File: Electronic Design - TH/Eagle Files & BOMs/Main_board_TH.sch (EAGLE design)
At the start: 46 parts, among them IC2 ATMEGA328-PU, X1 16MHz

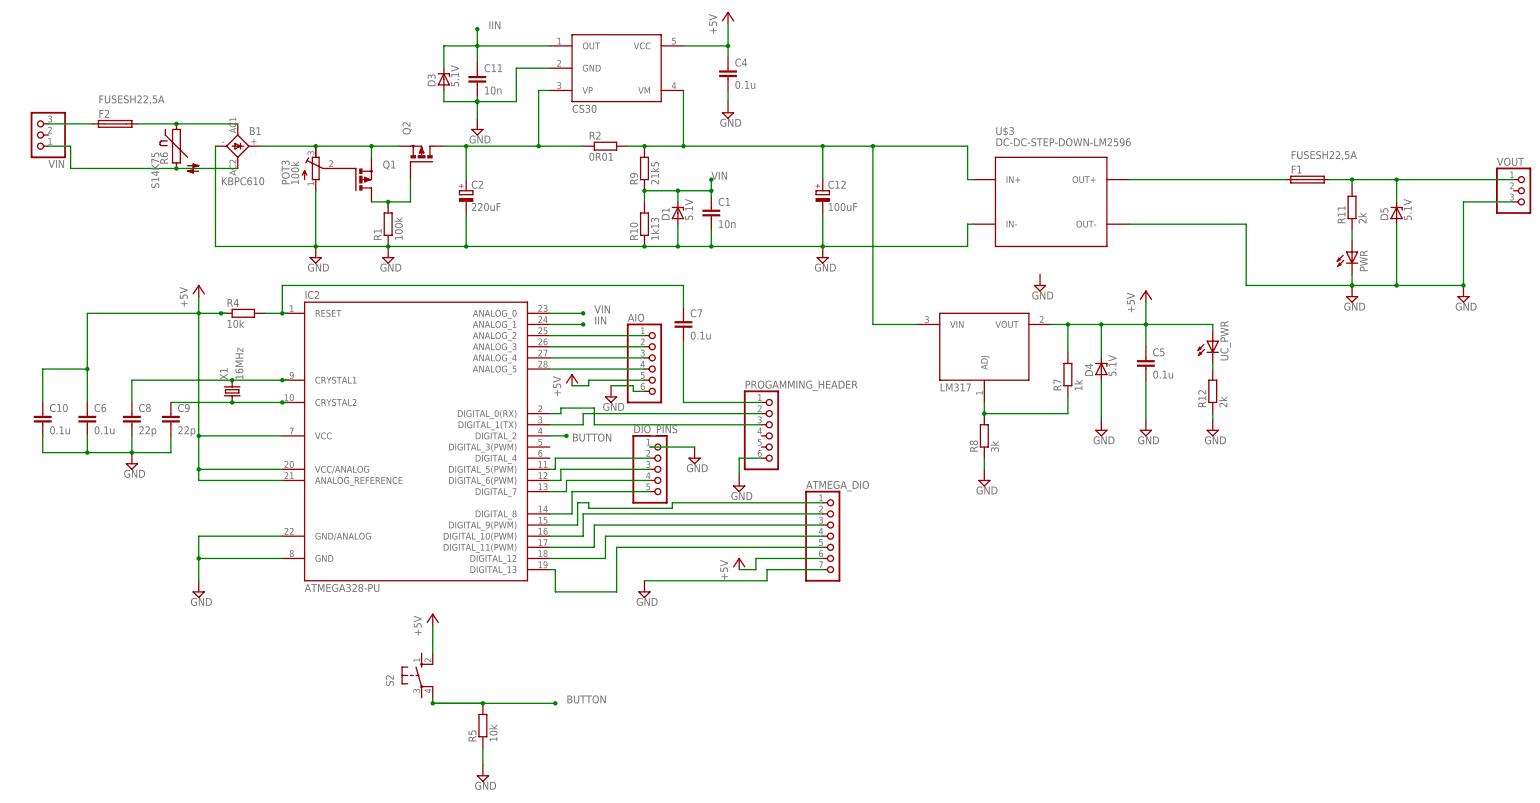
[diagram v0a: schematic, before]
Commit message: renamed files to reflect two versions of L.E.One and replacing ATmega 328 with arduino nano
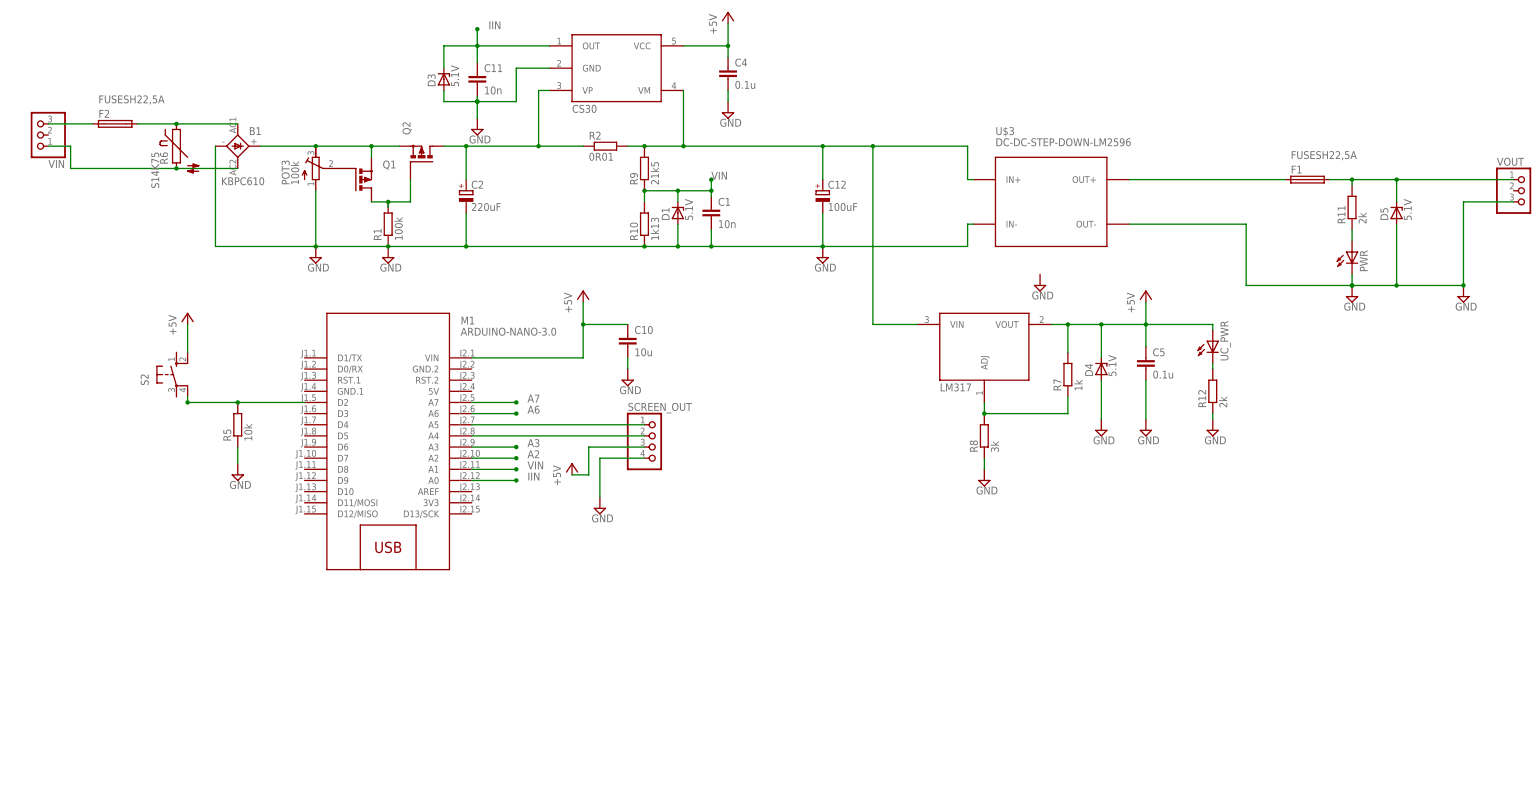
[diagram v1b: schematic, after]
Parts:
- removed AIO, PROGAMMING_HEADER: (no value), pinhead:PINHD-1X6
- removed ATMEGA_DIO: (no value), pinhead:PINHD-1X7
- removed C6, C7: 0.1u, resistor:C-EU050-024X044
- removed C8, C9: 22p, resistor:C-EU050-024X044
- removed DIO_PINS: (no value), pinhead:PINHD-1X5
- removed IC2: ATMEGA328-PU, Arduino-AVR:ATMEGA168-PU
- removed R4: 10k, resistor:R-EU_0207/10
- removed X1: 16MHz, crystal:CRYSTALHC49S
- added M1: ARDUINO-NANO-3.0, diy-modules:ARDUINO-NANO-3.0
- added SCREEN_OUT: (no value), pinhead:PINHD-1X4
- C10: value 0.1u -> 10u
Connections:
- removed net ANALOG_2: AIO.1, IC2.ANALOG_2
- removed net ANALOG_3: AIO.2, IC2.ANALOG_3
- removed net ANALOG_4: AIO.3, IC2.ANALOG_4
- removed net ANALOG_5: AIO.4, IC2.ANALOG_5
- removed net CRYSTAL1: C8.1, IC2.CRYSTAL1, X1.2
- removed net CRYSTAL2: C9.1, IC2.CRYSTAL2, X1.1
- removed net D10: ATMEGA_DIO.2, IC2.DIGITAL_10(PWM)
- removed net D11: ATMEGA_DIO.3, IC2.DIGITAL_11(PWM)
- removed net D12: ATMEGA_DIO.4, IC2.DIGITAL_12
- removed net D13: ATMEGA_DIO.5, IC2.DIGITAL_13
- removed net D5: DIO_PINS.2, IC2.DIGITAL_5(PWM)
- removed net D6: DIO_PINS.3, IC2.DIGITAL_6(PWM)
- removed net D7: DIO_PINS.4, IC2.DIGITAL_7
- removed net D8: DIO_PINS.5, IC2.DIGITAL_8
- removed net D9: ATMEGA_DIO.1, IC2.DIGITAL_9(PWM)
- removed net N$14: C7.2, PROGAMMING_HEADER.1
- removed net N$4: IC2.DIGITAL_1(TX), PROGAMMING_HEADER.2
- removed net N$5: IC2.DIGITAL_0(RX), PROGAMMING_HEADER.3
- removed net RESET: C7.1, IC2.RESET, R4.2
- new net A2: M1.A2
- new net A3: M1.A3
- new net A6: M1.A6
- new net A7: M1.A7
- new net N$2: M1.A4, SCREEN_OUT.2
- new net N$3: M1.A5, SCREEN_OUT.1
- net +5V: now also M1.VIN, SCREEN_OUT.3; no longer AIO.5, ATMEGA_DIO.6, C6.1, IC2.ANALOG_REFERENCE, IC2.VCC, IC2.VCC/ANALOG, R4.1
- net BUTTON: now also M1.D2; no longer IC2.DIGITAL_2
- net GND: now also SCREEN_OUT.4; no longer AIO.6, ATMEGA_DIO.7, C6.2, C8.2, C9.2, DIO_PINS.1, IC2.GND, IC2.GND/ANALOG, PROGAMMING_HEADER.6
- net IIN: no longer IC2.ANALOG_1
- net VIN: no longer IC2.ANALOG_0
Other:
- moved on the sheet: C10, R5, S2

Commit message: replacing CS30 with LM358
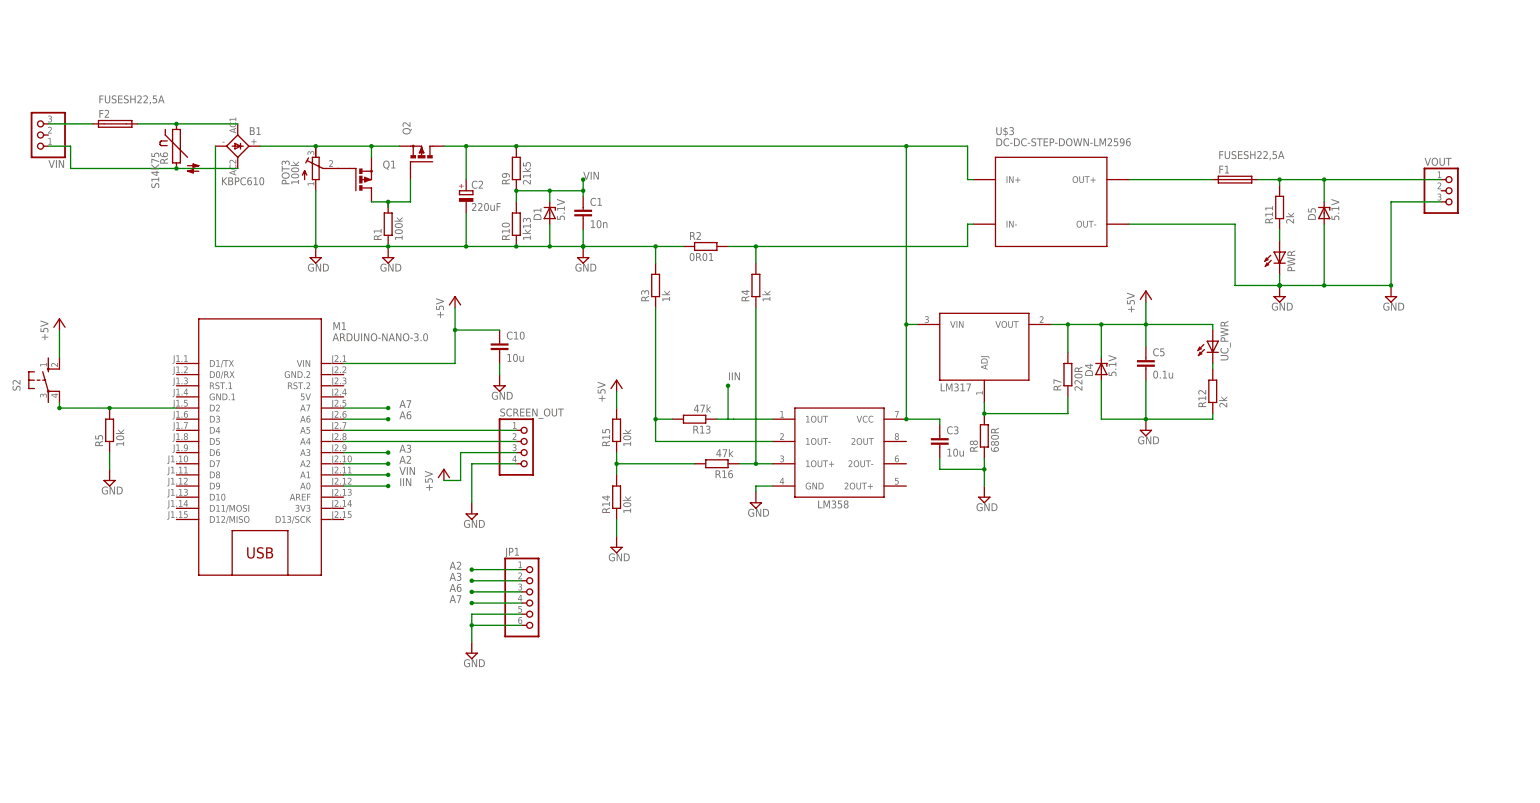
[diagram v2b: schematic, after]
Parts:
- removed C11: 10n, resistor:C-EU050-024X044
- removed C12: 100uF, resistor:CPOL-EUE3.5-8
- removed C4: 0.1u, resistor:C-EU050-024X044
- removed D3: 5.1V, diode:ZPD
- added C3: 10u, resistor:C-EU050-024X044
- added JP1: (no value), pinhead:PINHD-1X6
- added R13, R16: 47k, resistor:R-EU_0207/10
- added R14, R15: 10k, resistor:R-EU_0207/10
- added R3, R4: 1k, resistor:R-EU_0207/10
- R7: value 1k -> 220R
- R8: value 3k -> 680R
- U$2: value CS30 -> LM358; device Samson:CS30 -> Samson:LM358
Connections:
- removed net VIN_CURRENT_MEASURED: C12.+, R2.2, R9.2, U$1.VIN, U$2.VM, U$3.IN+
- new net N$4: R2.2, R4.2, U$3.IN-
- new net N$5: R16.1, R4.1, U$2.1OUT+
- new net N$6: R13.2, R3.1, U$2.1OUT-
- new net N$8: R14.2, R15.1, R16.2
- net +5V: now also R15.2; no longer C4.1, U$2.VCC
- net A2: now also JP1.1
- net A3: now also JP1.2
- net A6: now also JP1.3
- net A7: now also JP1.4
- net GND: now also C3.2, JP1.5, JP1.6, R14.1, R2.1, R3.2; no longer C11.2, C12.-, C4.2, D3.A, U$3.IN-
- net IIN: now also M1.A0, R13.1, U$2.1OUT; no longer C11.1, D3.C, U$2.OUT
- net VIN: now also M1.A1
- net VIN_PROTECTED: now also C3.1, R9.2, U$1.VIN, U$2.VCC, U$3.IN+; no longer R2.1, U$2.VP
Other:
- moved on the sheet: C1, C10, D1, D5, F1, M1, PWR, R10, R11, R2, R5, R9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

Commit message: replacing divider resistors for voltage measurement
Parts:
- R10: value 1k13 -> 1k
- R9: value 21k5 -> 10k
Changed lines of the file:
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@@
 <part name="C5" library="resistor" deviceset="C-EU" device="050-024X044" value="0.1u"/>
 <part name="SUPPLY11" library="supply2" deviceset="GND" device=""/>
-<part name="R9" library="resistor" deviceset="R-EU_" device="0207/10" value="21k5"/>
-<part name="R10" library="resistor" deviceset="R-EU_" device="0207/10" value="1k13"/>
+<part name="R9" library="resistor" deviceset="R-EU_" device="0207/10" value="10k"/>
+<part name="R10" library="resistor" deviceset="R-EU_" device="0207/10" value="1k"/>
 <part name="SUPPLY12" library="supply2" deviceset="GND" device=""/>
 <part name="D4" library="diode" deviceset="ZPD" device="" value="5.1V"/>

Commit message: Adding names of Q1 and Q2
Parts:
- Q1, Q2: value (none) -> IRF9520
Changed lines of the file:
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@@
 <setting verticaltext="up"/>
 </settings>
-<grid distance="0.05" unitdist="inch" unit="inch" style="lines" multiple="1" display="no" altdistance="0.01" altunitdist="inch" altunit="inch"/>
+<grid distance="0.1" unitdist="inch" unit="inch" style="lines" multiple="1" display="no" altdistance="0.01" altunitdist="inch" altunit="inch"/>
 <layers>
 <layer number="1" name="Top" color="4" fill="1" visible="no" active="no"/>
@@
 <part name="R11" library="resistor" deviceset="R-EU_" device="0207/10" value="2k"/>
 <part name="R12" library="resistor" deviceset="R-EU_" device="0207/10" value="2k"/>
-<part name="Q1" library="Samson" deviceset="PMOSFET_P" device="TO220BH"/>
-<part name="Q2" library="Samson" deviceset="PMOSFET_P" device="TO220BH"/>
+<part name="Q1" library="Samson" deviceset="PMOSFET_P" device="TO220BH" value="IRF9520"/>
+<part name="Q2" library="Samson" deviceset="PMOSFET_P" device="TO220BH" value="IRF9520"/>
 <part name="F2" library="fuse" deviceset="FUSE" device="SH22,5A" value="FUSESH22,5A"/>
 <part name="U$3" library="diy-modules" deviceset="DC-DC-STEP-DOWN-LM2596" device=""/>

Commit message: adding ground to arduino
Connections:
- net GND: now also M1.GND.2
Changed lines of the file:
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@@
 <setting verticaltext="up"/>
 </settings>
-<grid distance="0.1" unitdist="inch" unit="inch" style="lines" multiple="1" display="no" altdistance="0.01" altunitdist="inch" altunit="inch"/>
+<grid distance="0.05" unitdist="inch" unit="inch" style="lines" multiple="1" display="no" altdistance="0.01" altunitdist="inch" altunit="inch"/>
 <layers>
 <layer number="1" name="Top" color="4" fill="1" visible="no" active="no"/>
@@
 <part name="SUPPLY5" library="supply2" deviceset="GND" device=""/>
 <part name="C3" library="resistor" deviceset="C-EU" device="050-024X044" value="10u"/>
+<part name="SUPPLY6" library="supply2" deviceset="GND" device=""/>
 </parts>
 <sheets>
@@
 <instance part="SUPPLY5" gate="GND" x="-30.48" y="-26.67"/>
 <instance part="C3" gate="G$1" x="76.2" y="22.86"/>
+<instance part="SUPPLY6" gate="GND" x="-34.29" y="33.02"/>
 </instances>
 <busses>
@@
 <junction x="27.94" y="34.29"/>
 <label x="27.94" y="35.56" size="1.778" layer="95"/>
+<junction x="27.94" y="26.67"/>
 </segment>
 </net>
@@
 <junction x="-30.48" y="-20.32"/>
 </segment>
+<segment>
+<pinref part="M1" gate="G$1" pin="GND.2"/>
+<pinref part="SUPPLY6" gate="GND" pin="GND"/>
+<wire x1="-59.69" y1="36.83" x2="-34.29" y2="36.83" width="0.1524" layer="91"/>
+<wire x1="-34.29" y1="36.83" x2="-34.29" y2="35.56" width="0.1524" layer="91"/>
+</segment>
 </net>

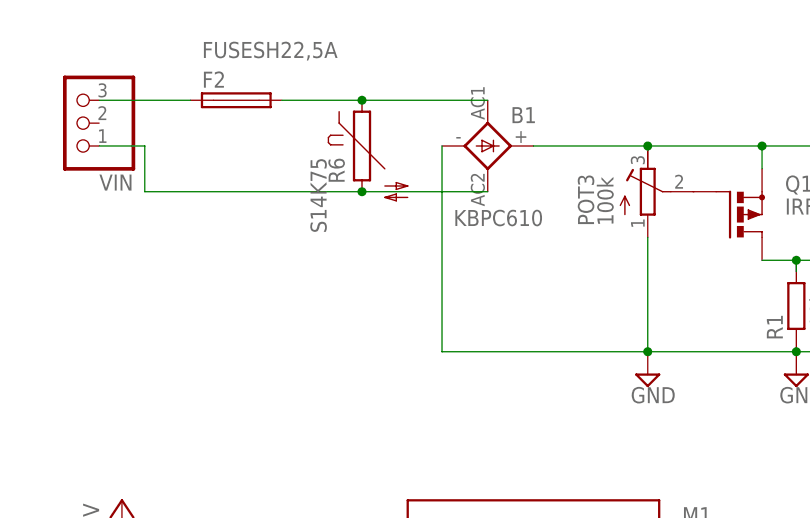
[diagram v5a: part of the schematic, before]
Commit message: Moving varistor to after rectification stage
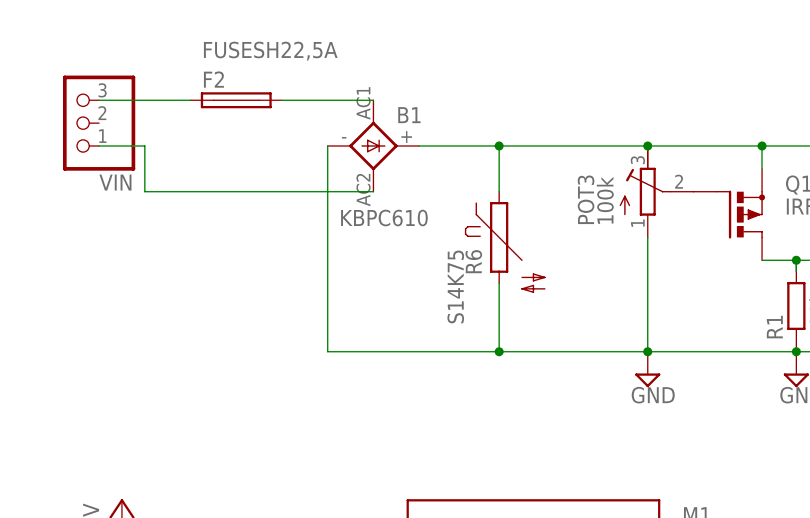
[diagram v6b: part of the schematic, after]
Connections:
- removed net VIN_AC1: B1.AC1, F2.2, R6.1
- removed net VIN_AC2: B1.AC2, R6.2, VIN.1
- new net N$7: B1.AC2, VIN.1
- new net N$9: B1.AC1, F2.2
- net GND: now also R6.2
- net VIN_UNPROTECTED: now also R6.1
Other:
- moved on the sheet: B1, R6
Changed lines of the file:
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@@
 </plain>
 <instances>
-<instance part="B1" gate="1" x="-83.82" y="88.9" smashed="yes">
-<attribute name="NAME" x="-81.28" y="91.44" size="1.778" layer="95"/>
-<attribute name="VALUE" x="-87.63" y="80.01" size="1.778" layer="96"/>
+<instance part="B1" gate="1" x="-96.52" y="88.9" smashed="yes">
+<attribute name="NAME" x="-93.98" y="91.44" size="1.778" layer="95"/>
+<attribute name="VALUE" x="-100.33" y="80.01" size="1.778" layer="96"/>
 </instance>
 <instance part="C1" gate="G$1" x="-5.08" y="74.93"/>
@@
 <instance part="SUPPLY3" gate="GND" x="-113.03" y="12.7"/>
 <instance part="D1" gate="G$1" x="-12.7" y="73.66" rot="R90"/>
-<instance part="R6" gate="G$1" x="-97.79" y="88.9" rot="R270"/>
+<instance part="R6" gate="G$1" x="-82.55" y="78.74" rot="R270"/>
 <instance part="SUPPLY2" gate="GND" x="179.07" y="54.61"/>
 <instance part="SUPPLY4" gate="GND" x="86.36" y="8.89"/>
@@
 <junction x="-66.04" y="66.04"/>
 <pinref part="B1" gate="1" pin="-"/>
-<wire x1="-88.9" y1="88.9" x2="-88.9" y2="66.04" width="0.1524" layer="91"/>
-<wire x1="-66.04" y1="66.04" x2="-88.9" y2="66.04" width="0.1524" layer="91"/>
+<wire x1="-101.6" y1="88.9" x2="-101.6" y2="66.04" width="0.1524" layer="91"/>
+<wire x1="-66.04" y1="66.04" x2="-82.55" y2="66.04" width="0.1524" layer="91"/>
+<wire x1="-82.55" y1="66.04" x2="-101.6" y2="66.04" width="0.1524" layer="91"/>
 <wire x1="-12.7" y1="66.04" x2="-5.08" y2="66.04" width="0.1524" layer="91"/>
 <wire x1="-12.7" y1="71.12" x2="-12.7" y2="66.04" width="0.1524" layer="91"/>
@@
 <wire x1="11.43" y1="62.23" x2="11.43" y2="66.04" width="0.1524" layer="91"/>
 <junction x="11.43" y="66.04"/>
+<pinref part="R6" gate="G$1" pin="2"/>
+<wire x1="-82.55" y1="73.66" x2="-82.55" y2="66.04" width="0.1524" layer="91"/>
+<junction x="-82.55" y="66.04"/>
 </segment>
 <segment>
@@
 <pinref part="B1" gate="1" pin="+"/>
 <wire x1="-53.34" y1="88.9" x2="-46.99" y2="88.9" width="0.1524" layer="91"/>
-<wire x1="-78.74" y1="88.9" x2="-66.04" y2="88.9" width="0.1524" layer="91"/>
+<wire x1="-91.44" y1="88.9" x2="-82.55" y2="88.9" width="0.1524" layer="91"/>
 <junction x="-66.04" y="88.9"/>
 <pinref part="Q2" gate="G$1" pin="S"/>
 <pinref part="Q1" gate="G$1" pin="S"/>
+<wire x1="-82.55" y1="88.9" x2="-66.04" y2="88.9" width="0.1524" layer="91"/>
 <wire x1="-53.34" y1="86.36" x2="-53.34" y2="88.9" width="0.1524" layer="91"/>
 <junction x="-53.34" y="88.9"/>
+<pinref part="R6" gate="G$1" pin="1"/>
+<wire x1="-82.55" y1="88.9" x2="-82.55" y2="83.82" width="0.1524" layer="91"/>
+<junction x="-82.55" y="88.9"/>
 </segment>
 </net>
@@
 </segment>
 </net>
-<net name="VIN_AC2" class="0">
-<segment>
-<pinref part="VIN" gate="A" pin="1"/>
-<wire x1="-127" y1="88.9" x2="-121.92" y2="88.9" width="0.1524" layer="91"/>
-<wire x1="-121.92" y1="88.9" x2="-121.92" y2="83.82" width="0.1524" layer="91"/>
-<pinref part="R6" gate="G$1" pin="2"/>
-<wire x1="-121.92" y1="83.82" x2="-97.79" y2="83.82" width="0.1524" layer="91"/>
-<pinref part="B1" gate="1" pin="AC2"/>
-<wire x1="-97.79" y1="83.82" x2="-83.82" y2="83.82" width="0.1524" layer="91"/>
-<junction x="-97.79" y="83.82"/>
-</segment>
-</net>
 <net name="N$23" class="0">
 <segment>
@@
 </segment>
 </net>
-<net name="VIN_AC1" class="0">
-<segment>
-<pinref part="R6" gate="G$1" pin="1"/>
-<pinref part="B1" gate="1" pin="AC1"/>
-<wire x1="-83.82" y1="93.98" x2="-97.79" y2="93.98" width="0.1524" layer="91"/>
-<pinref part="F2" gate="G$1" pin="2"/>
-<wire x1="-106.68" y1="93.98" x2="-97.79" y2="93.98" width="0.1524" layer="91"/>
-<junction x="-97.79" y="93.98"/>
-</segment>
-</net>
 <net name="VOUT_PREFUSE" class="0">
 <segment>
@@
 </segment>
 </net>
+<net name="N$7" class="0">
+<segment>
+<pinref part="VIN" gate="A" pin="1"/>
+<wire x1="-127" y1="88.9" x2="-121.92" y2="88.9" width="0.1524" layer="91"/>
+<wire x1="-121.92" y1="88.9" x2="-121.92" y2="83.82" width="0.1524" layer="91"/>
+<pinref part="B1" gate="1" pin="AC2"/>
+<wire x1="-121.92" y1="83.82" x2="-96.52" y2="83.82" width="0.1524" layer="91"/>
+</segment>
+</net>
+<net name="N$9" class="0">
+<segment>
+<pinref part="B1" gate="1" pin="AC1"/>
+<pinref part="F2" gate="G$1" pin="2"/>
+<wire x1="-96.52" y1="93.98" x2="-106.68" y2="93.98" width="0.1524" layer="91"/>
+</segment>
+</net>
